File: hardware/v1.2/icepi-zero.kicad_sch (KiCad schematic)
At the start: 29 parts, among them J1 Conn_02x20_Counter_Clockwise, SW1 SW_Push, SW2 SW_Push, U1 ECP5-CABGA256, Y1 SITxxxxxx-1x-33E-50.000000

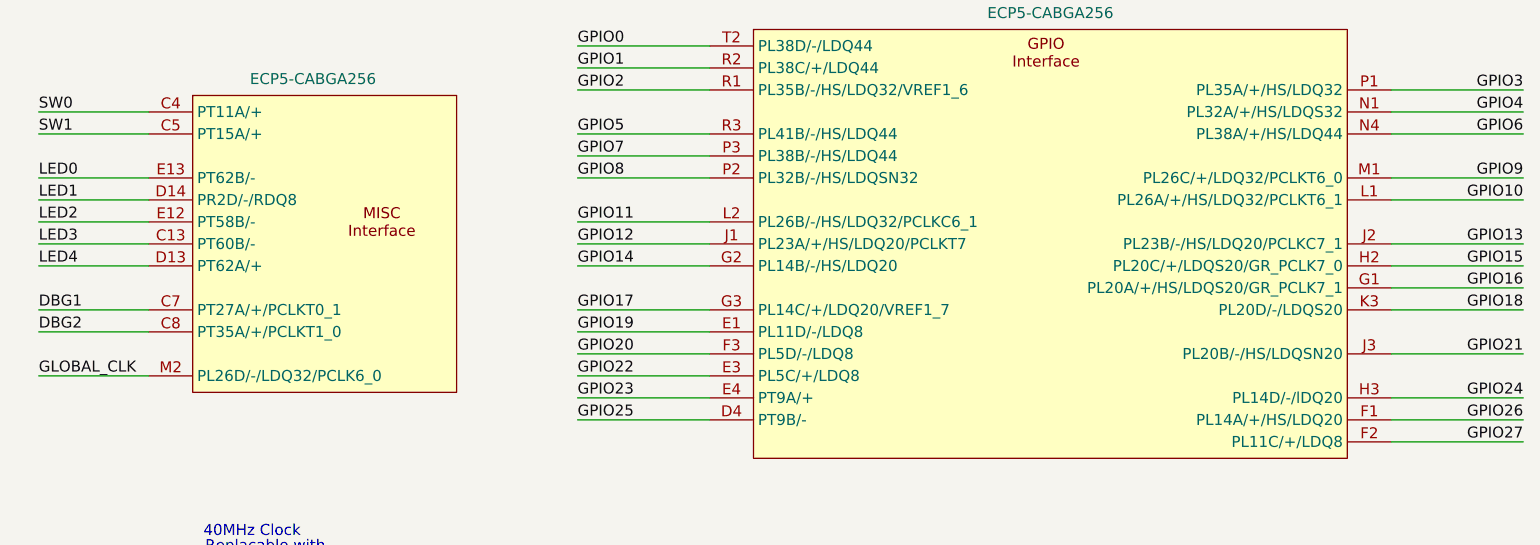
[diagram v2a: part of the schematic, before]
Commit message: Put better pin names for LPF files
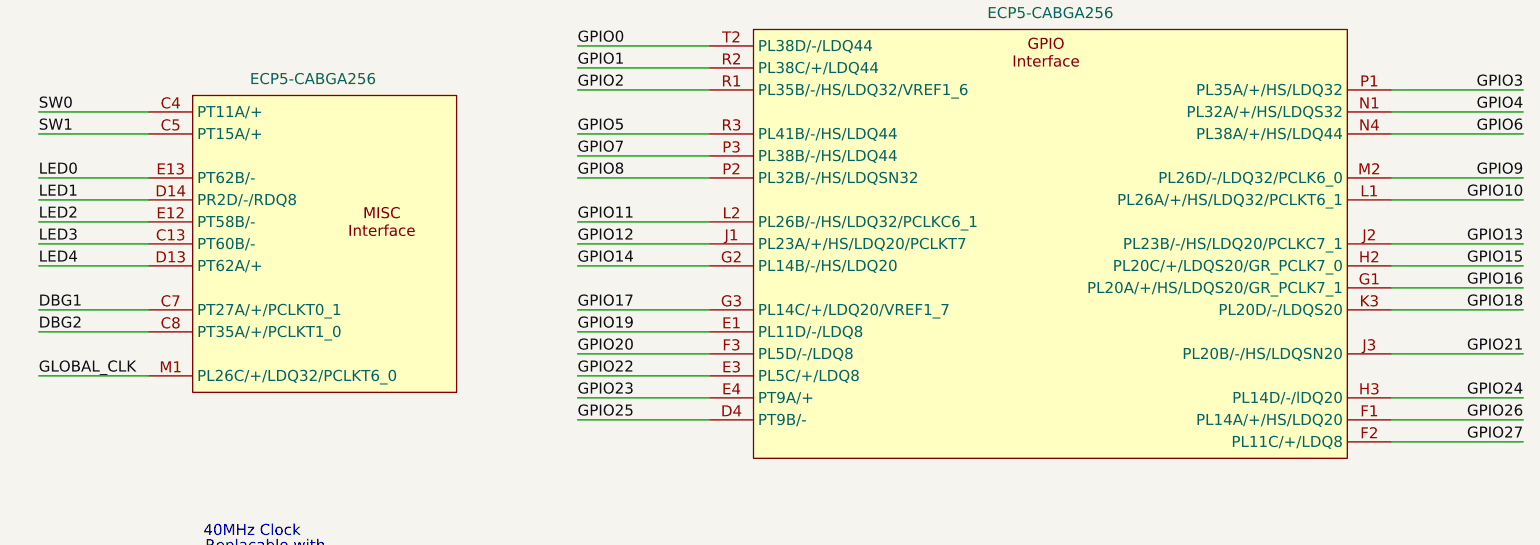
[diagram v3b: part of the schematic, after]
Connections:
- net GLOBAL_CLK: now also U1.M1 (PL26C/+/LDQ32/PCLKT6_0); no longer U1.M2 (PL26D/-/LDQ32/PCLK6_0)
- net GPIO9: now also U1.M2 (PL26D/-/LDQ32/PCLK6_0); no longer U1.M1 (PL26C/+/LDQ32/PCLKT6_0)
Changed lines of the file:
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@@
 	)
 	(symbol
+		(lib_name "LFE5U-25F-6BG256x_1")
 		(lib_id "icepi-lib:LFE5U-25F-6BG256x")
 		(at 170.18 119.38 0)

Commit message: Don't overwrite v1.2 with v1.3
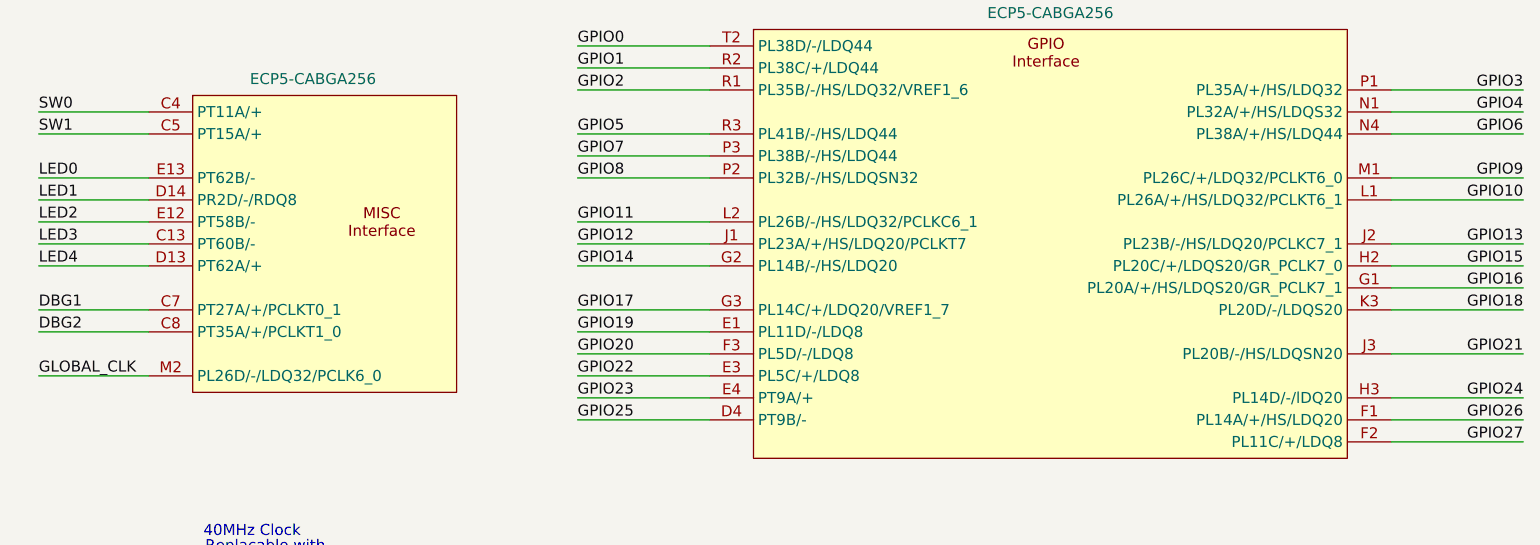
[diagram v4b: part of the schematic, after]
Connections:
- net GLOBAL_CLK: now also U1.M2 (PL26D/-/LDQ32/PCLK6_0); no longer U1.M1 (PL26C/+/LDQ32/PCLKT6_0)
- net GPIO9: now also U1.M1 (PL26C/+/LDQ32/PCLKT6_0); no longer U1.M2 (PL26D/-/LDQ32/PCLK6_0)
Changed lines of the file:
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@@
 	)
 	(symbol
-		(lib_name "LFE5U-25F-6BG256x_1")
 		(lib_id "icepi-lib:LFE5U-25F-6BG256x")
 		(at 170.18 119.38 0)

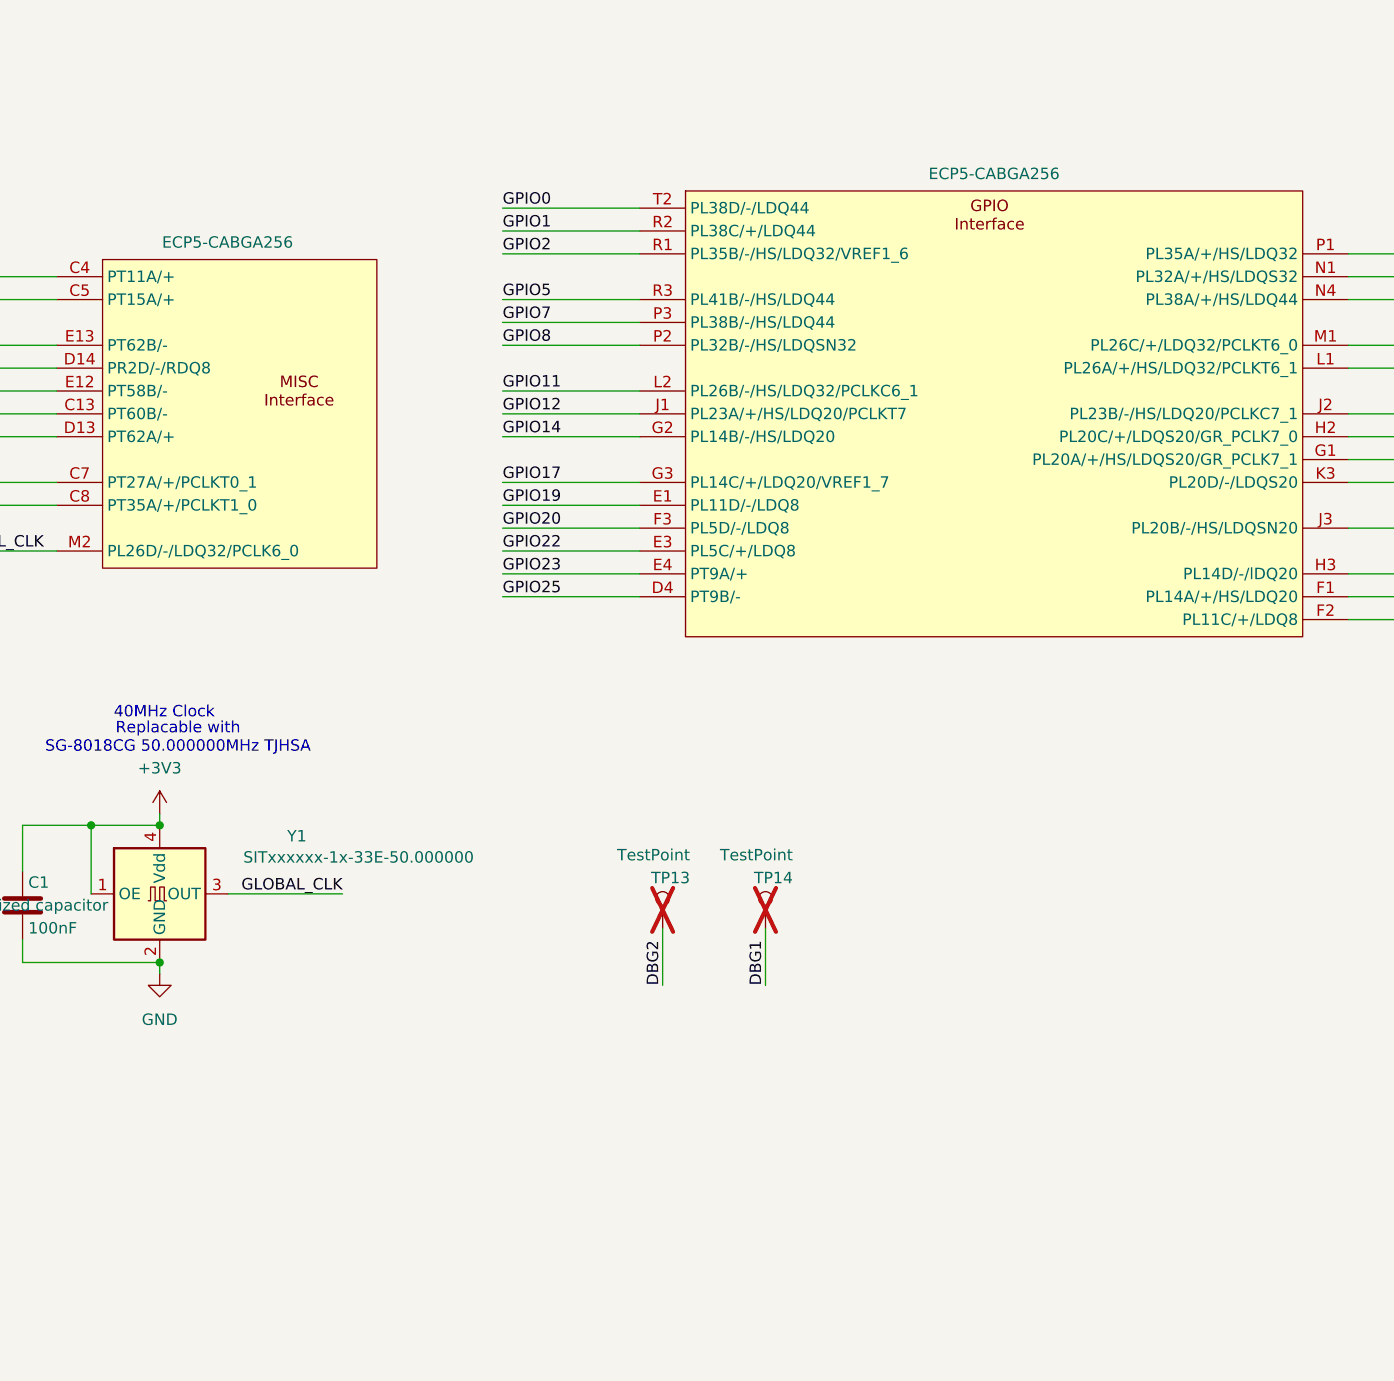
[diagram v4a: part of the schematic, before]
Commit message: UART to PS2 converter
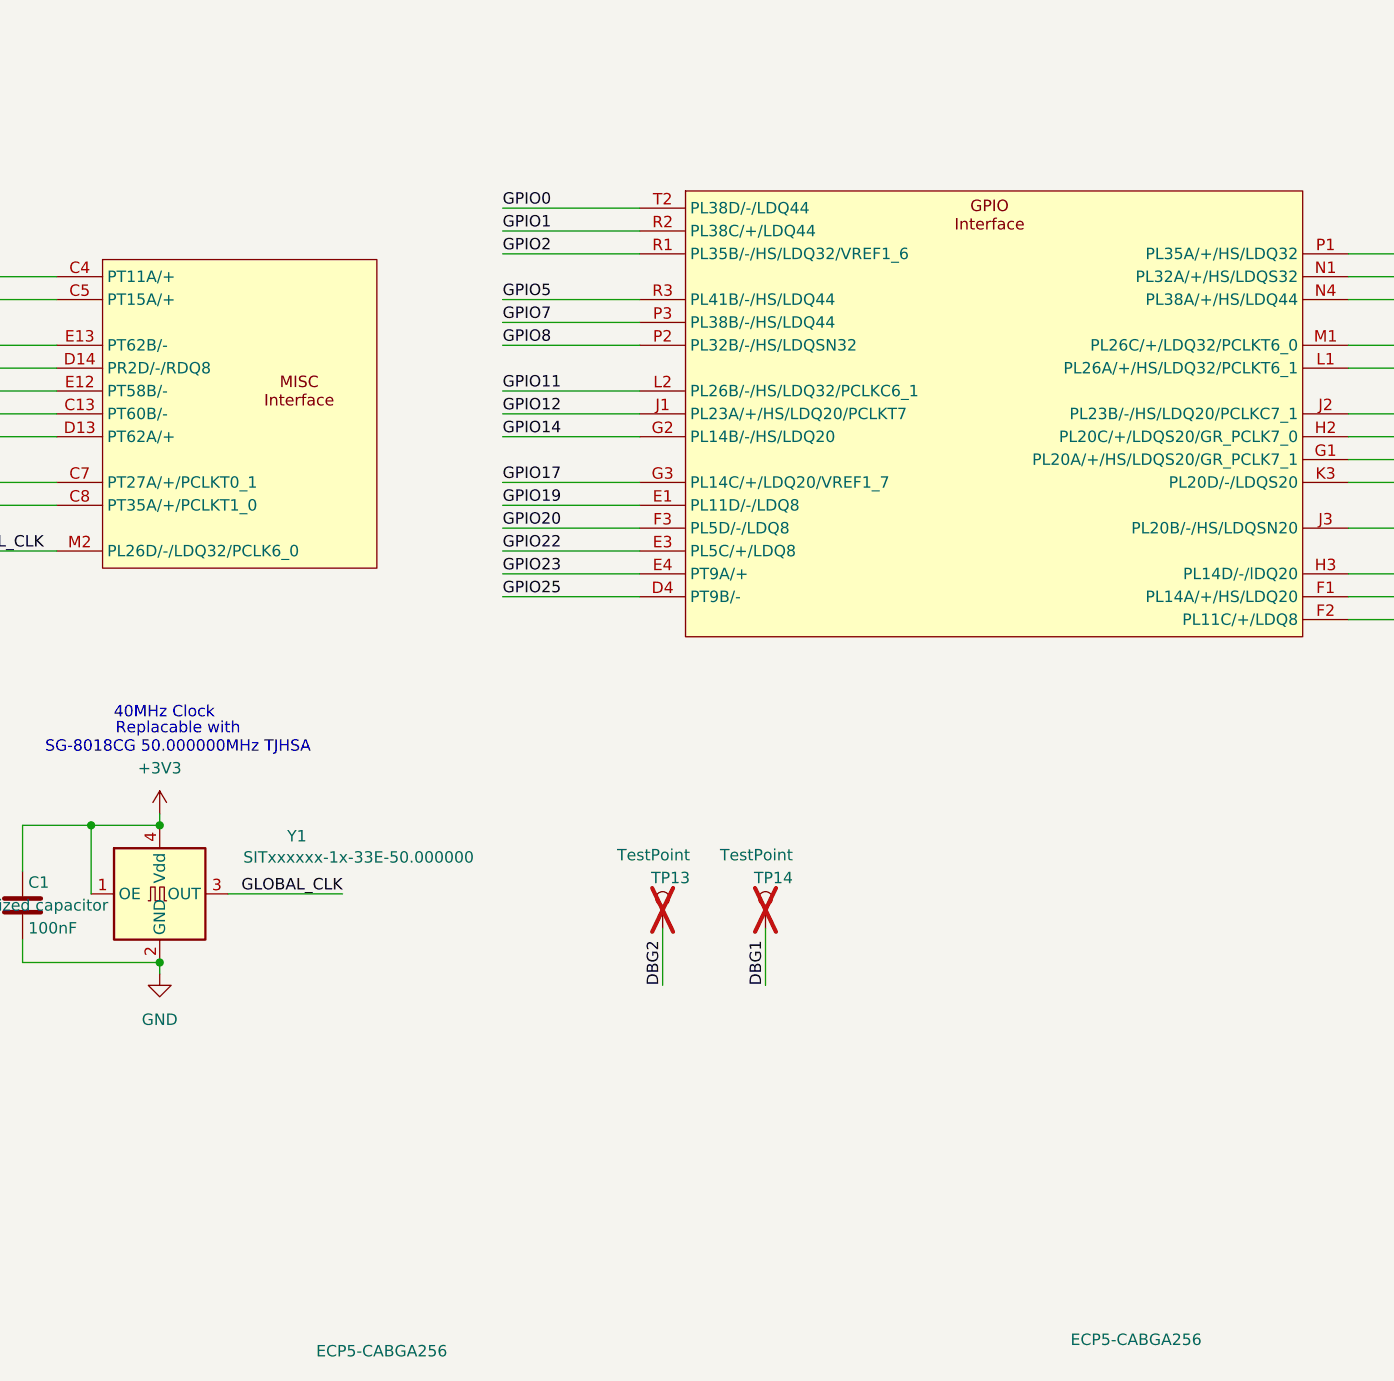
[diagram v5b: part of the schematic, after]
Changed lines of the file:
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@@
 		)
 		(property "Value" "ECP5-CABGA256"
-			(at 170.18 93.98 0)
-			(effects
-				(font
-					(size 1.27 1.27)
-				)
+			(at 178.6733 223.52 0)
+			(effects
+				(font
+					(size 1.27 1.27)
+				)
+				(justify left)
 			)
 		)
@@
 			(project "icepi-zero"
 				(path "/f88da08e-cf42-4d03-a08f-3f602fe6658d"
+					(reference "U1")
+					(unit 8)
+				)
+				(path "/f88da08e-cf42-4d03-a08f-3f602fe6658d/17c9c9b3-f379-4e1f-a876-d3fcf0529a4d"
 					(reference "U1")
 					(unit 8)
@@
 	)
 	(symbol
+		(lib_name "LFE5U-25F-6BG256x_1")
 		(lib_id "icepi-lib:LFE5U-25F-6BG256x")
 		(at 86.36 120.65 0)
@@
 		)
 		(property "Value" "ECP5-CABGA256"
-			(at 77.724 101.6 0)
+			(at 94.8533 224.79 0)
 			(effects
 				(font
@@
 					(reference "U1")
 					(unit 9)
+				)
+				(path "/f88da08e-cf42-4d03-a08f-3f602fe6658d/17c9c9b3-f379-4e1f-a876-d3fcf0529a4d"
+					(reference "U1")
+					(unit 9)

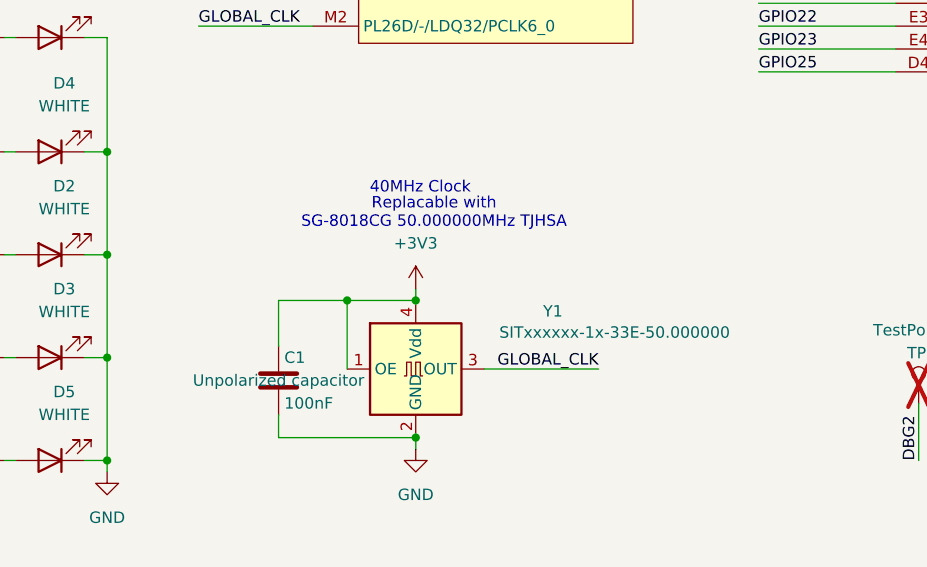
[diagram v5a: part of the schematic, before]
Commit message: Improve Makefile and v1.0 lpf
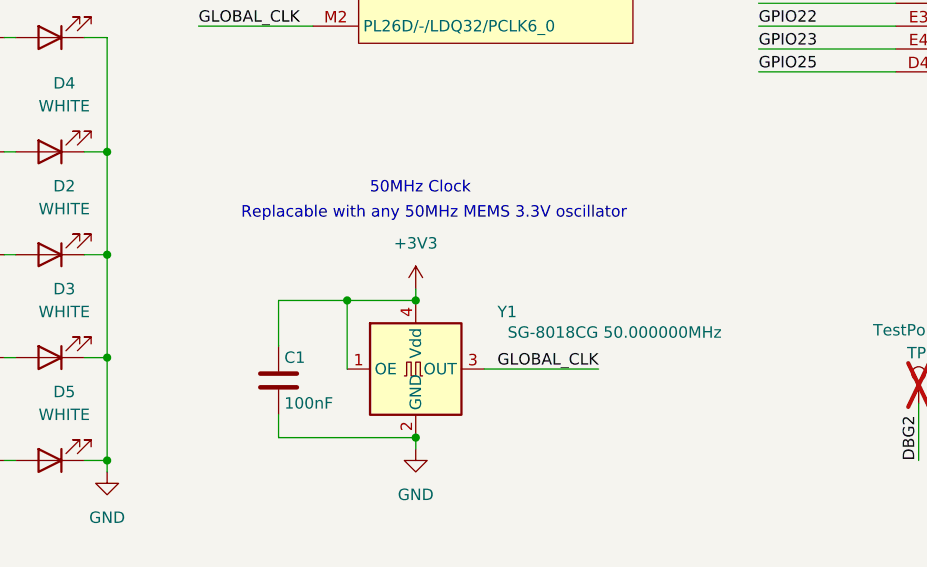
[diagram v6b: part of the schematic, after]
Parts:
- Y1: value SITxxxxxx-1x-33E-50.000000 -> SG-8018CG 50.000000MHz; LCSC Part # C1182928 -> C390526
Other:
- note added: "50MHz Clock"
- note added: "Replacable with any 50MHz MEMS 3.3V oscillator"
- note removed: "40MHz Clock"
- note removed: "Replacable with SG-8018CG 50.000000MHz TJHSA"
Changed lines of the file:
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@@
 		)
 	)
-	(text "Replacable with\nSG-8018CG 50.000000MHz TJHSA"
+	(text "Replacable with any 50MHz MEMS 3.3V oscillator"
 		(exclude_from_sim no)
 		(at 79.502 156.718 0)
@@
 		)
 	)
-	(text "40MHz Clock"
+	(text "50MHz Clock"
 		(exclude_from_sim no)
 		(at 77.978 153.924 0)
@@
 		(dnp no)
 		(property "Reference" "Y1"
-			(at 92.71 167.5698 0)
+			(at 87.63 167.64 0)
 			(effects
 				(font
@@
 			)
 		)
-		(property "Value" "SITxxxxxx-1x-33E-50.000000"
+		(property "Value" "SG-8018CG 50.000000MHz"
 			(at 99.568 169.926 0)
 			(effects
@@
 			)
 		)
-		(property "LCSC Part #" "C1182928"
+		(property "LCSC Part #" "C390526"
 			(at 77.47 173.99 0)
 			(effects
@@
 					(unit 8)
 				)
-				(path "/f88da08e-cf42-4d03-a08f-3f602fe6658d/17c9c9b3-f379-4e1f-a876-d3fcf0529a4d"
-					(reference "U1")
-					(unit 8)
-				)
 			)
 		)
@@
 					(unit 9)
 				)
-				(path "/f88da08e-cf42-4d03-a08f-3f602fe6658d/17c9c9b3-f379-4e1f-a876-d3fcf0529a4d"
-					(reference "U1")
-					(unit 9)
-				)
 			)
 		)
@@
 					(size 1.27 1.27)
 				)
+				(hide yes)
 			)
 		)
